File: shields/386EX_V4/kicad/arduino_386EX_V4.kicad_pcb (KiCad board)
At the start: 4 copper layers, 93.3 x 60.3 mm, 53 parts, among them J1 WP Jumper, J2 Conn_01x02_Pin, J3 Conn_01x04_Pin, J4 SERIAL0, J5 Conn_01x04_Pin, J6 Conn_01x04_Pin, J7 JTAG, U1 ULN2003A, U2 SN74LV14A, U3 AT24CS01-STUM, U4 I386EX_PQFP

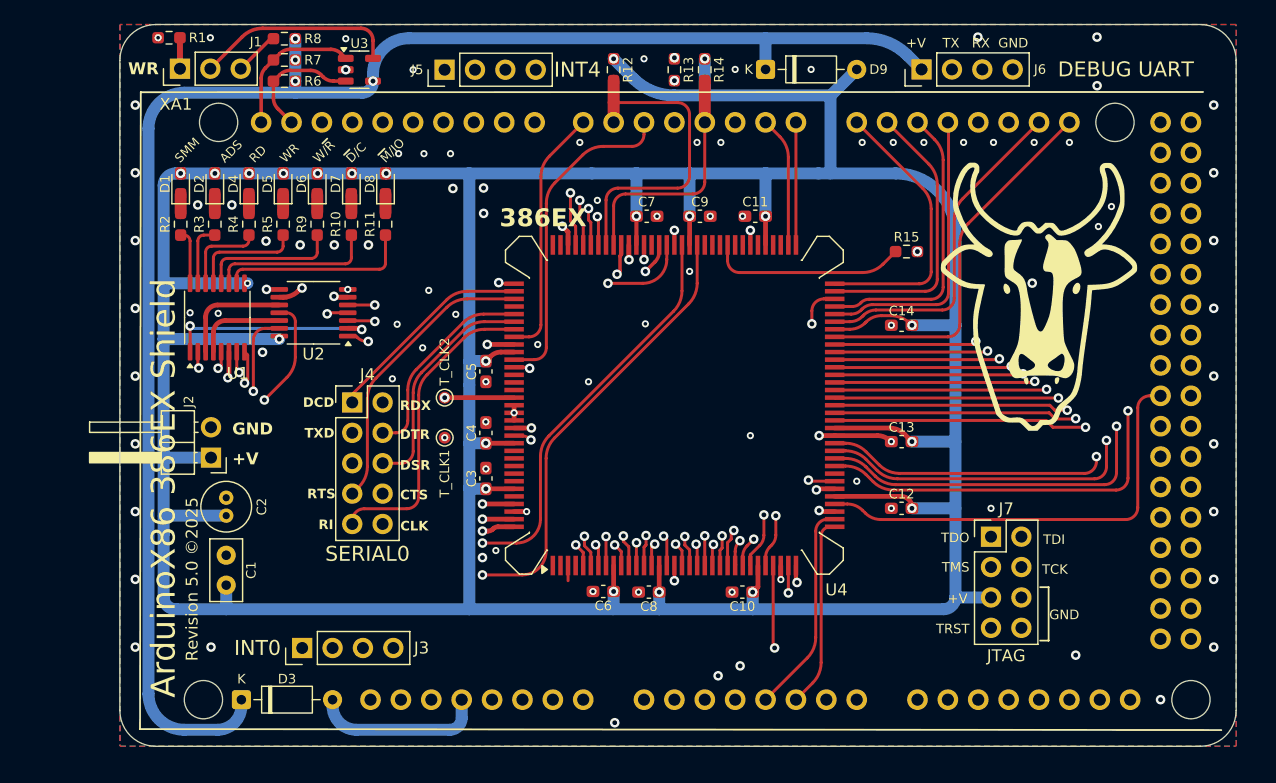
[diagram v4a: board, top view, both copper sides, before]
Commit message: Updated 386EX to rev 5.1; added LDL1117 LDO, swapped to SMD diodes, tidied schematic.
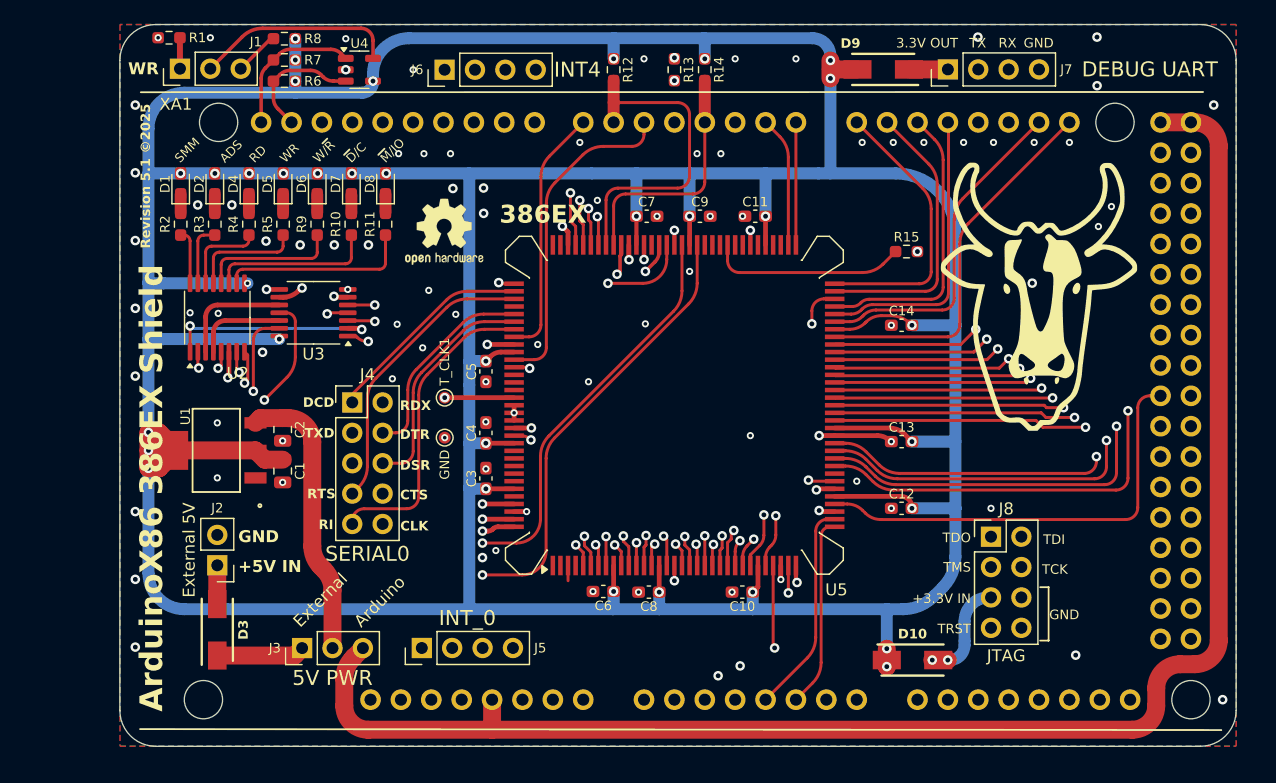
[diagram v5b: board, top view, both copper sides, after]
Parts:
- removed the T_CLK1 at (137.6, 98.7)
- added D3: S1A-13-F, Diodes Inc S1A-13-F 50V 1A standard diode:DIOM5226X240N, F.Cu at (118.6, 114.7)
- added GND: TestPoint, TestPoint:TestPoint_Pad_D1.0mm, F.Cu at (137.6, 98.7)
- added J3: WP Jumper, Connector_PinHeader_2.54mm:PinHeader_1x03_P2.54mm_Vertical, F.Cu at (125.7, 116.2)
- added REF**: OSHW-Logo2_7.3x6mm_SilkScreen, Symbol:OSHW-Logo2_7.3x6mm_SilkScreen, F.Cu at (137.6, 81.5)
- added U1: LDL1117S33R, ST LDL1117S33R 1A 3.3V LDO:SOT223_STM-M, F.Cu at (118.5, 99.7)
- C1: value C_Polarized -> 4.7 uF; footprint Capacitor_THT:C_Disc_D5.0mm_W2.5mm_P2.50mm -> Capacitor_SMD:C_0805_2012Metric
- C2: value C_Polarized -> 1 uF; footprint Capacitor_THT:C_Radial_D4.0mm_H5.0mm_P1.50mm -> Capacitor_SMD:C_0805_2012Metric
- D10: renamed from D3; value 1N4148 -> S1A-13-F; footprint Diode_THT:D_DO-35_SOD27_P7.62mm_Horizontal -> Diodes Inc S1A-13-F 50V 1A standard diode:DIOM5226X240N
- D9: value 1N4148 -> S1A-13-F; footprint Diode_THT:D_DO-35_SOD27_P7.62mm_Horizontal -> Diodes Inc S1A-13-F 50V 1A standard diode:DIOM5226X240N
- J2: footprint Connector_PinHeader_2.54mm:PinHeader_1x02_P2.54mm_Horizontal -> Connector_PinHeader_2.54mm:PinHeader_1x02_P2.54mm_Vertical
- moved D10 56.2 mm to (176.8, 117.2)
- moved C1 10.6 mm to (124.1, 101.4), turned to -90 degrees
- moved J5 10.00 mm to (135.7, 116.2)
- moved D9 9.84 mm to (174.3, 67.9), turned to 180 degrees
- moved J2 9.02 mm to (118.6, 109.3)
- moved C2 8.61 mm to (124.1, 98.0), turned to -90 degrees
- moved J7 2.20 mm to (179.7, 67.9)
- renumbered J3 to J5, J5 to J6, J6 to J7, J7 to J8, T_CLK2 to T_CLK1, U1 to U2, U2 to U3, U3 to U4, U4 to U5
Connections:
- C1 pad 1: +3.3VP -> 3.3V_LOCAL
- C10 pad 2: +3.3VP -> 3.3V_LOCAL
- C11 pad 2: +3.3VP -> 3.3V_LOCAL
- C12 pad 2: +3.3VP -> 3.3V_LOCAL
- C13 pad 2: +3.3VP -> 3.3V_LOCAL
- C14 pad 2: +3.3VP -> 3.3V_LOCAL
- C2 pad 1: +3.3VP -> PWR_SELECTED
- C3 pad 2: +3.3VP -> 3.3V_LOCAL
- C4 pad 2: +3.3VP -> 3.3V_LOCAL
- C5 pad 2: +3.3VP -> 3.3V_LOCAL
- C6 pad 2: +3.3VP -> 3.3V_LOCAL
- C7 pad 2: +3.3VP -> 3.3V_LOCAL
- C8 pad 2: +3.3VP -> 3.3V_LOCAL
- C9 pad 2: +3.3VP -> 3.3V_LOCAL
- D1 pad 2: +3.3VP -> 3.3V_LOCAL
- D10 pad 1: 3.3V_COMBINED -> 3.3V_LOCAL
- D10 pad 2: +3.3V -> Net-(D3-A)
- D2 pad 2: +3.3VP -> 3.3V_LOCAL
- D4 pad 2: +3.3VP -> 3.3V_LOCAL
- D5 pad 2: +3.3VP -> 3.3V_LOCAL
- D6 pad 2: +3.3VP -> 3.3V_LOCAL
- D7 pad 2: +3.3VP -> 3.3V_LOCAL
- D8 pad 2: +3.3VP -> 3.3V_LOCAL
- D9 pad 1: 3.3V_COMBINED -> Net-(D9-K)
- D9 pad 2: +3.3VP -> 3.3V_LOCAL
- J2 pad 1: +3.3VP -> Net-(D10-A)
- J7 pad 1: 3.3V_COMBINED -> Net-(D9-K)
- J8 pad 5: +3.3VP -> Net-(D3-A)
- R12 pad 2: +3.3VP -> 3.3V_LOCAL
- R14 pad 2: +3.3VP -> 3.3V_LOCAL
- R6 pad 2: 3.3V_COMBINED -> 3.3V_LOCAL
- R7 pad 2: 3.3V_COMBINED -> 3.3V_LOCAL
- R8 pad 2: 3.3V_COMBINED -> 3.3V_LOCAL
- U2 pad 9: +3.3VP -> 3.3V_LOCAL
- U3 pad 14: +3.3VP -> 3.3V_LOCAL
- U4 pad 4: 3.3V_COMBINED -> 3.3V_LOCAL
- U5 pad 109: +3.3VP -> 3.3V_LOCAL
- U5 pad 121: +3.3VP -> 3.3V_LOCAL
- U5 pad 127: +3.3VP -> 3.3V_LOCAL
- U5 pad 15: +3.3VP -> 3.3V_LOCAL
- U5 pad 28: +3.3VP -> 3.3V_LOCAL
- U5 pad 38: +3.3VP -> 3.3V_LOCAL
- U5 pad 47: +3.3VP -> 3.3V_LOCAL
- U5 pad 60: +3.3VP -> 3.3V_LOCAL
- U5 pad 71: +3.3VP -> 3.3V_LOCAL
- U5 pad 81: +3.3VP -> 3.3V_LOCAL
- U5 pad 88: +3.3VP -> 3.3V_LOCAL
- U5 pad 9: +3.3VP -> 3.3V_LOCAL
- XA1 pad 3V3: +3.3V -> ARDUINO_3.3V
- XA1 pad 5V1: unconnected-(XA1-5V-Pad5V1) -> ARDUINO_5V
- XA1 pad 5V3: unconnected-(XA1-5V-Pad5V3) -> ARDUINO_5V
- XA1 pad 5V4: unconnected-(XA1-5V-Pad5V4) -> ARDUINO_5V
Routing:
- net 3.3V_LOCAL: track 0.00 -> 445.5 mm, vias 0 -> 34
- net +3.3VP: track 373.6 -> 0.00 mm, vias 23 -> 0
- net 3.3V_COMBINED: track 135.1 -> 0.00 mm, vias 4 -> 0
- net ARDUINO_5V: track 0.00 -> 133.9 mm
- net PWR_SELECTED: track 0.00 -> 23.7 mm
- net +3.3V: track 14.4 -> 0.00 mm
- net INT3: track 50.3 -> 40.3 mm
- net Net-(D3-A): track 0.00 -> 9.92 mm, vias 0 -> 2
- net EXT_5V: track 0.00 -> 7.35 mm
- net INT0: track 54.4 -> 47.7 mm
- net INT1: track 49.5 -> 44.4 mm
- net Net-(D9-K): track 0.00 -> 3.26 mm
- net INT2: track 50.6 -> 47.3 mm
- net Net-(D10-A): track 0.00 -> 2.86 mm
- net /A14_A: track 41.2 -> 42.9 mm
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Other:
- board text added: "+3.3V IN"
- board text added: "+5V IN"
- board text added: "3.3V OUT"
- board text added: "5V PWR"
- board text added: "Arduino"
- board text added: "External"
- board text added: "External 5V"
- board text added: "INT_0"
- board text added: "Revision 5.1 ©2025"
- board text removed: "+V"
- board text removed: "INT0"
- board text removed: "Revision 5.0 ©2025"

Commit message: Reverted 386EX_V4 to track with original fork of repo.
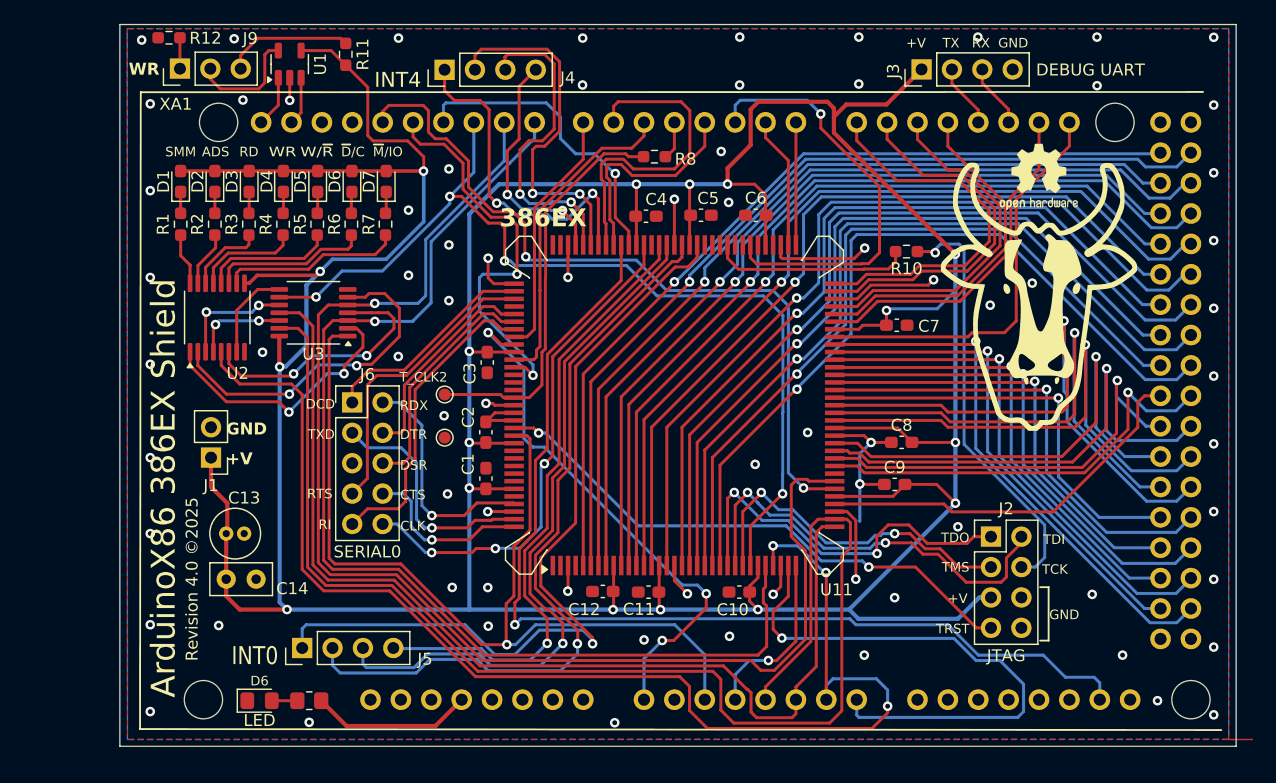
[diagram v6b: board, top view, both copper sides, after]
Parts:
- removed the C1 at (124.1, 101.4)
- removed the C2 at (124.1, 98.0)
- removed D10, D9: S1A-13-F, Diodes Inc S1A-13-F 50V 1A standard diode:DIOM5226X240N
- removed the D3 at (118.6, 114.7)
- removed GND: TestPoint, TestPoint:TestPoint_Pad_D1.0mm
- removed the J3 at (125.7, 116.2)
- removed the R12 at (151.8, 67.9)
- removed R14: 3.3 K Ohm, Resistor_SMD:R_0603_1608Metric_Pad0.98x0.95mm_HandSolder
- removed the R7 at (124.2, 67.1)
- removed the U1 at (118.5, 99.7)
- added C13: C_Polarized, Capacitor_THT:C_Radial_D4.0mm_H5.0mm_P1.50mm, F.Cu at (119.4, 106.7)
- added C14: C_Polarized, Capacitor_THT:C_Disc_D5.0mm_W2.5mm_P2.50mm, F.Cu at (119.4, 110.5)
- added D6: LED, LED_SMD:LED_0805_2012Metric_Pad1.15x1.40mm_HandSolder, F.Cu at (122.2, 120.7)
- added T_CLK2_GND1: TestPoint, TestPoint:TestPoint_Pad_D1.0mm, F.Cu at (137.6, 98.7)
- C1: renamed from C3; value 0.1 uF -> C
- C10: value 0.1 uF -> C
- C11: renamed from C8; value 0.1 uF -> C
- C12: renamed from C6; value 0.1 uF -> C
- C2: renamed from C4; value 0.1 uF -> C
- C3: renamed from C5; value 0.1 uF -> C
- C4: renamed from C7; value 0.1 uF -> C
- C5: renamed from C9; value 0.1 uF -> C
- C6: renamed from C11; value 0.1 uF -> C
- C7: renamed from C14; value 0.1 uF -> C
- C8: renamed from C13; value 0.1 uF -> C
- C9: renamed from C12; value 0.1 uF -> C
- R11: renamed from R8; value 3.3 K Ohm -> R
- R12: renamed from R1; value 3.3 K Ohm -> R
- R6: value 3.3 K Ohm -> 750Ω; footprint Resistor_SMD:R_0603_1608Metric_Pad0.98x0.95mm_HandSolder -> Resistor_SMD:R_0805_2012Metric_Pad1.20x1.40mm_HandSolder
- moved R6 51.8 mm to (126.3, 120.7), turned to 180 degrees
- moved REF** 49.9 mm to (187.3, 76.9)
- moved J5 10.00 mm to (125.7, 116.2)
- moved J1 9.02 mm to (118.1, 100.3)
- moved R8 7.46 mm to (155.2, 75.2), turned to 180 degrees
- moved U1 5.84 mm to (124.7, 67.4), turned to 90 degrees
- moved R11 5.29 mm to (129.4, 66.6), turned to -90 degrees
- moved J3 2.20 mm to (177.5, 67.9)
- moved C9 2.08 mm to (175.3, 102.6)
- moved C3 0.76 mm to (141.2, 92.4)
- moved C7 0.40 mm to (175.4, 89.3), turned to 180 degrees
- moved T_CLK2 0.26 mm to (137.6, 95.1)
- moved C10 0.25 mm to (162.3, 111.6)
- moved D7 0.21 mm to (132.8, 77.2)
- moved D6 0.21 mm to (129.9, 77.2)
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- renumbered D4 to D3, D5 to D4, D6 to D5, D7 to D6, D8 to D7, J2 to J1, J8 to J2, J7 to J3, J6 to J4, J4 to J6, J1 to J9, R2 to R1, R15 to R10, R3 to R2, R4 to R3, R5 to R4, R9 to R5, R10 to R6, R11 to R7, R13 to R8, T_CLK1 to T_CLK2, U4 to U1, U5 to U11
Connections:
- C1 pad 2: 3.3V_LOCAL -> +3.3VP
- C10 pad 2: 3.3V_LOCAL -> +3.3VP
- C11 pad 2: 3.3V_LOCAL -> +3.3VP
- C12 pad 2: 3.3V_LOCAL -> +3.3VP
- C2 pad 2: 3.3V_LOCAL -> +3.3VP
- C3 pad 2: 3.3V_LOCAL -> +3.3VP
- C4 pad 2: 3.3V_LOCAL -> +3.3VP
- C5 pad 2: 3.3V_LOCAL -> +3.3VP
- C6 pad 2: 3.3V_LOCAL -> +3.3VP
- C7 pad 2: 3.3V_LOCAL -> +3.3VP
- C8 pad 2: 3.3V_LOCAL -> +3.3VP
- C9 pad 2: 3.3V_LOCAL -> +3.3VP
- D1 pad 2: 3.3V_LOCAL -> +3.3VP
- D2 pad 2: 3.3V_LOCAL -> +3.3VP
- D3 pad 2: 3.3V_LOCAL -> +3.3VP
- D4 pad 2: 3.3V_LOCAL -> +3.3VP
- D5 pad 2: 3.3V_LOCAL -> +3.3VP
- D6 pad 2: 3.3V_LOCAL -> +3.3VP
- D7 pad 2: 3.3V_LOCAL -> +3.3VP
- J1 pad 1: Net-(D10-A) -> +3.3VP
- J2 pad 5: Net-(D3-A) -> +3.3VP
- J3 pad 1: Net-(D9-K) -> +3.3VP
- R11 pad 2: 3.3V_LOCAL -> +3.3VP
- R6 pad 1: SDA -> +3.3V
- R6 pad 2: 3.3V_LOCAL -> Net-(D6-A)
- U1 pad 4: 3.3V_LOCAL -> +3.3VP
- U11 pad 109: 3.3V_LOCAL -> +3.3VP
- U11 pad 121: 3.3V_LOCAL -> +3.3VP
- U11 pad 127: 3.3V_LOCAL -> +3.3VP
- U11 pad 15: 3.3V_LOCAL -> +3.3VP
- U11 pad 28: 3.3V_LOCAL -> +3.3VP
- U11 pad 38: 3.3V_LOCAL -> +3.3VP
- U11 pad 47: 3.3V_LOCAL -> +3.3VP
- U11 pad 60: 3.3V_LOCAL -> +3.3VP
- U11 pad 71: 3.3V_LOCAL -> +3.3VP
- U11 pad 81: 3.3V_LOCAL -> +3.3VP
- U11 pad 88: 3.3V_LOCAL -> +3.3VP
- U11 pad 9: 3.3V_LOCAL -> +3.3VP
- U2 pad 9: 3.3V_LOCAL -> +3.3VP
- U3 pad 14: 3.3V_LOCAL -> +3.3VP
- XA1 pad 3V3: ARDUINO_3.3V -> +3.3V
- XA1 pad 5V1: ARDUINO_5V -> unconnected-(XA1-5V-Pad5V1)
- XA1 pad 5V3: ARDUINO_5V -> unconnected-(XA1-5V-Pad5V3)
- XA1 pad 5V4: ARDUINO_5V -> unconnected-(XA1-5V-Pad5V4)
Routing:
- net 3.3V_LOCAL: track 445.5 -> 0.00 mm, vias 34 -> 0
- net +3.3VP: track 0.00 -> 373.4 mm, vias 0 -> 17
- net ARDUINO_5V: track 133.9 -> 0.00 mm
- net ~{ADS}: track 61.5 -> 110.4 mm, vias 3 -> 1
- net GND: track 24.4 -> 68.2 mm, vias 91 -> 76
- net ~{READY}: track 13.5 -> 46.5 mm
- net D/~{C}: track 64.3 -> 95.5 mm, vias 3 -> 1
- net ~{SMIACT}: track 51.3 -> 79.3 mm, vias 2 -> 1
- net ~{SMI}: track 10.7 -> 35.3 mm
- net PWR_SELECTED: track 23.7 -> 0.00 mm
- net INT0: track 47.7 -> 69.7 mm
- net NMI: track 66.6 -> 88.2 mm
- net INT1: track 44.4 -> 64.6 mm
- net W/~{R}: track 86.3 -> 106.2 mm, vias 2 -> 3
- net ~{WR}: track 91.8 -> 109.6 mm, vias 2 -> 0
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- removed copper zone on In1.Cu, net GND
- removed copper zone on In2.Cu, net GND
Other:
- outline, holes or cut-outs redrawn
- copper layers 4 -> 2
- board text added: "+V"
- board text added: "INT0"
- board text added: "Revision 4.0 ©2025"
- board text removed: "+3.3V IN"
- board text removed: "+5V IN"
- board text removed: "3.3V OUT"
- board text removed: "5V PWR"
- board text removed: "Arduino"
- board text removed: "External"
- board text removed: "External 5V"
- board text removed: "INT_0"
- board text removed: "Revision 5.1 ©2025"

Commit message: Revert added files in shields/386ex_v4/
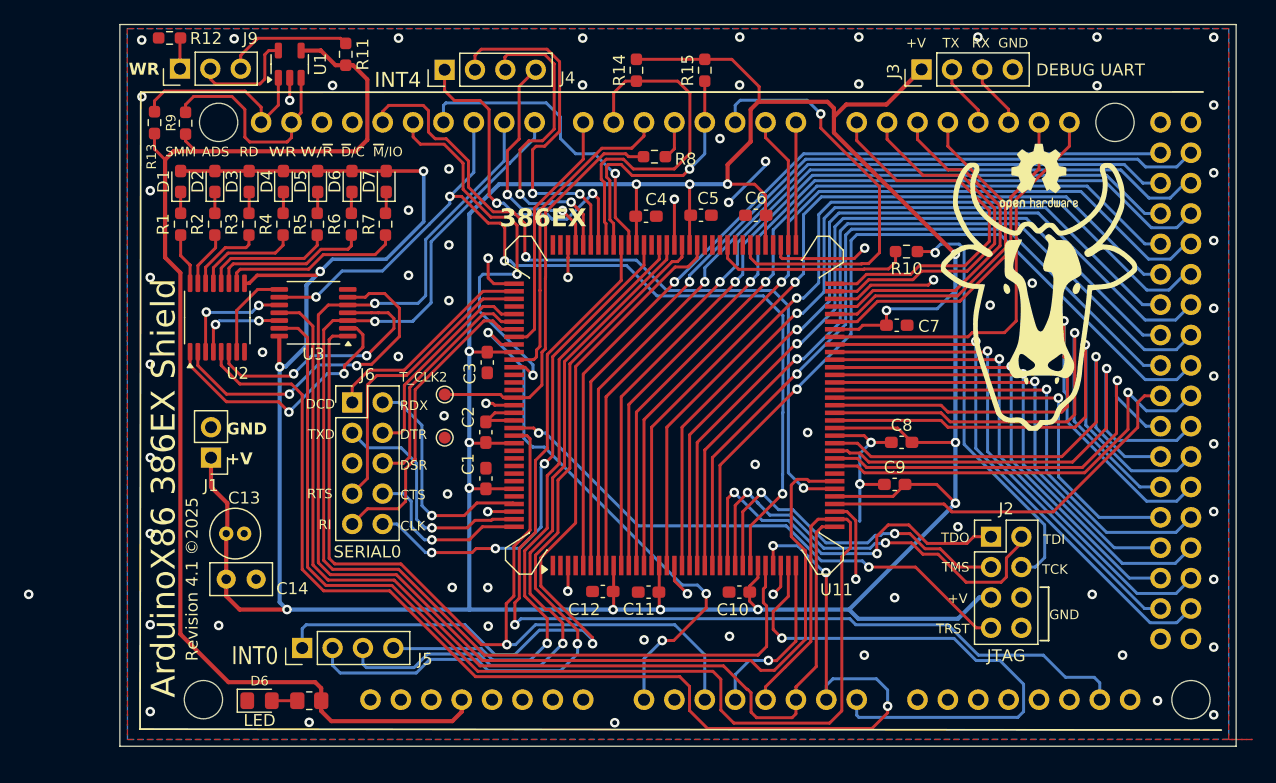
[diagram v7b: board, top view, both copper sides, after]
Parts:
- added R13: R, Resistor_SMD:R_0603_1608Metric_Pad0.98x0.95mm_HandSolder, F.Cu at (113.4, 72.3)
- added R14: R, Resistor_SMD:R_0603_1608Metric_Pad0.98x0.95mm_HandSolder, F.Cu at (153.7, 67.9)
- added R15: R, Resistor_SMD:R_0603_1608Metric_Pad0.98x0.95mm_HandSolder, F.Cu at (159.4, 67.9)
- added R9: R, Resistor_SMD:R_0603_1608Metric_Pad0.98x0.95mm_HandSolder, F.Cu at (116.0, 72.4)
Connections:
- R11 pad 2: +3.3VP -> +3.3V
- U1 pad 4: +3.3VP -> +3.3V
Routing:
- net +3.3V: track 13.5 -> 102.7 mm
- net SDA: track 4.06 -> 18.2 mm
- net SCL: track 4.32 -> 16.3 mm
- net +3.3VP: track 373.4 -> 368.3 mm
- net GND: track 68.2 -> 72.9 mm, vias 76 -> 77
- net ~{ERROR}: track 18.5 -> 22.3 mm, vias 0 -> 1
- net ~{BUSY}: track 27.1 -> 30.1 mm
- net /WP: track 9.59 -> 9.07 mm
- net (no net): vias 0 -> 1
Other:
- board text added: "Revision 4.1 ©2025"
- board text removed: "Revision 4.0 ©2025"
